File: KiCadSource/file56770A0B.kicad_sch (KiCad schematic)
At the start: 60 parts, among them Q1 BSS138BKS, Q2 BSS138BKS, U1 ADA4817-1, U2 ADA4817-1

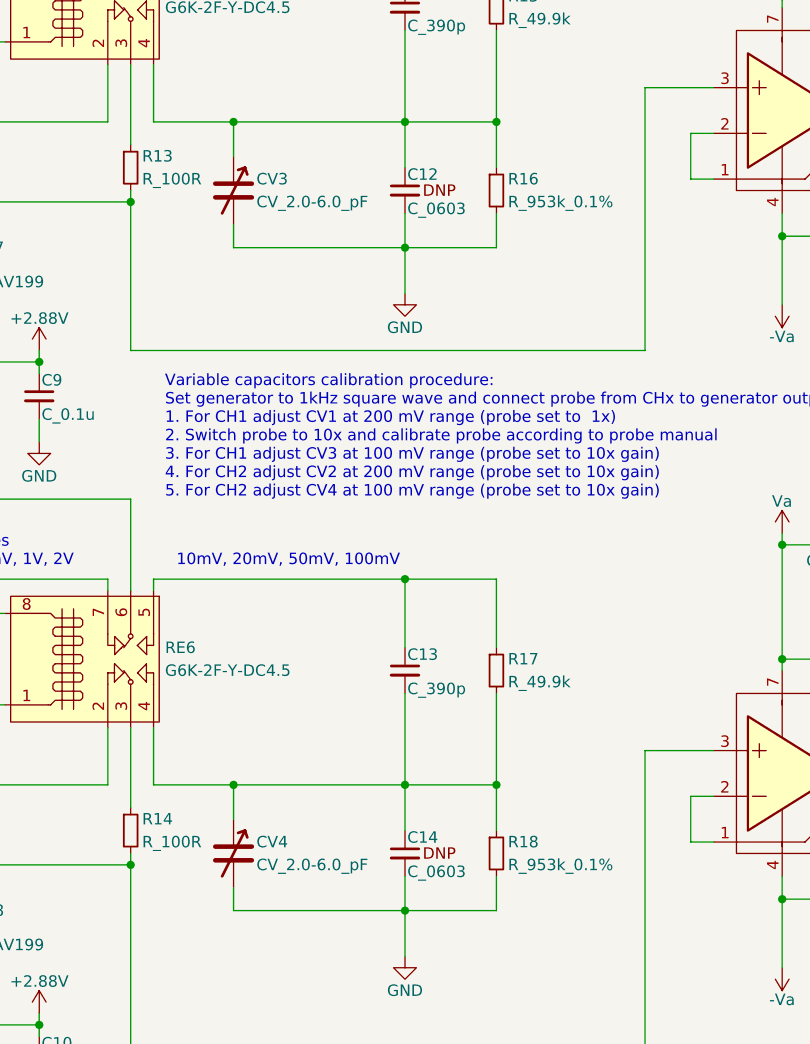
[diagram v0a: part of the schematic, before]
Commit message: updating part attributes
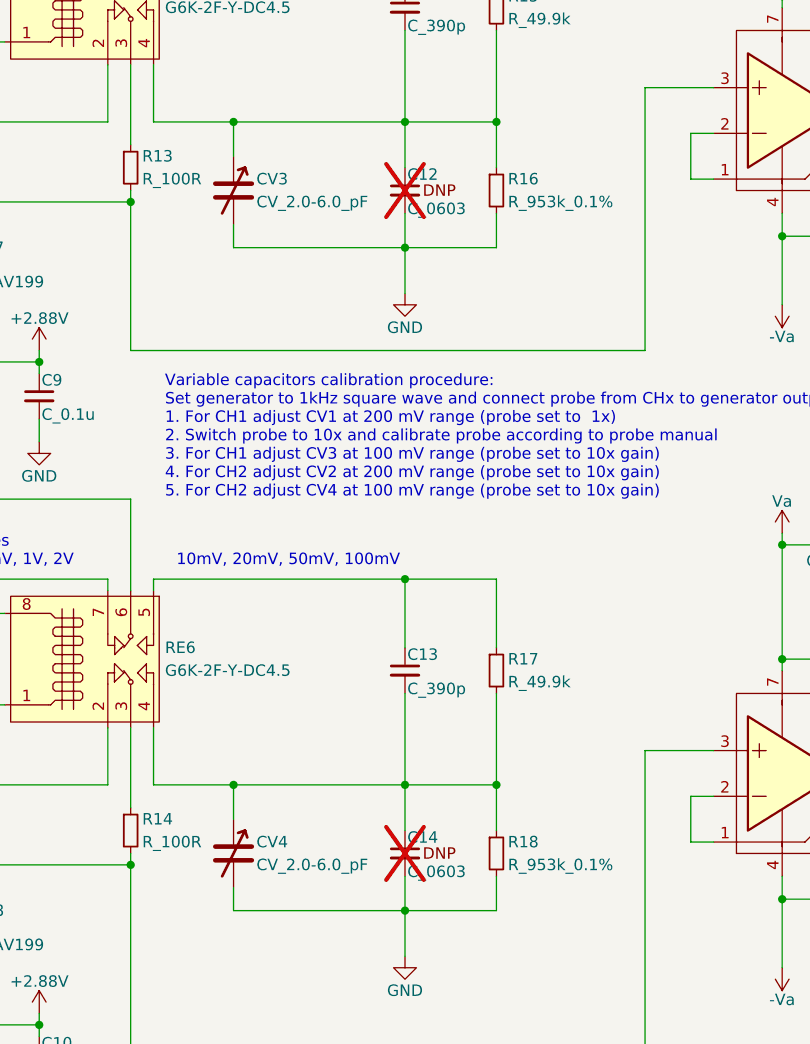
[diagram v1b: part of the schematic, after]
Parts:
- C12, C14: now not fitted
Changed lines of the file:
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@@
 		(in_bom yes)
 		(on_board yes)
-		(dnp no)
+		(dnp yes)
 		(property "Reference" "C14"
 			(at 212.344 126.492 0)
@@
 		(in_bom yes)
 		(on_board yes)
-		(dnp no)
+		(dnp yes)
 		(property "Reference" "C12"
 			(at 212.344 52.832 0)
